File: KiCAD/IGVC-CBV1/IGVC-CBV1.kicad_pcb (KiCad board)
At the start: 2 copper layers, 9.8 x 4.5 mm, 42 parts, among them IC1 STM32F407ZGT6, IC2 SPX3819M5-L-3-3_TR, IC3 AT45DB081E-SSHN-B, J1 STLINKV2 PINS (2.54mm Pitch), J2 Motor Driver Pins (2.54mm Pit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, J3 12401948E412A, J4 Conn_01x02, SW1 SW_SPDT, Y1 EB2532YA12-25.000M_TR

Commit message: placed some things where they need to go
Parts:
- IC2, J4: moved to B.Cu
- moved J1 88.7 mm to (223.2, 80.2), turned to 90 degrees
- moved J2 87.9 mm to (223.1, 92.9), turned to 90 degrees
- moved IC3 72.1 mm to (222.9, 68.1), turned to 90 degrees
- moved R6 68.2 mm to (220.8, 62.9), turned to 90 degrees
- moved SW1 68.1 mm to (200.9, 60.1), turned to 90 degrees
- moved R7 64.8 mm to (222.3, 73.3), turned to 90 degrees
- moved R5 61.7 mm to (220.9, 73.3), turned to 90 degrees
- moved IC1 59.1 mm to (196.8, 89.6)
- moved C18 45.3 mm to (187.0, 72.6), turned to -90 degrees
- moved C22 41.2 mm to (119.4, 81.6), turned to -90 degrees
- moved C17 39.9 mm to (181.7, 72.6), turned to -90 degrees
- moved IC2 36.5 mm to (177.6, 102.3)
- moved C24 32.3 mm to (181.3, 104.5), turned to -90 degrees
- moved C23 32.3 mm to (181.3, 100.4), turned to -90 degrees
- moved FB1 28.1 mm to (184.4, 72.3)
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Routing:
- added copper zone on B.Cu, net (none)
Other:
- board size 9.8 x 4.5 mm -> 4.5 x 9.8 mm

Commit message: finished layout
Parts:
- R8: moved to B.Cu
- moved C22 107.0 mm to (224.1, 59.7), turned to 180 degrees
- moved R8 92.7 mm to (227.7, 68.0), turned to 90 degrees
- moved C21 83.8 mm to (224.1, 61.8), turned to 180 degrees
- moved R1 58.8 mm to (191.4, 72.5), turned to -90 degrees
- moved C1 46.6 mm to (133.3, 71.4), turned to -90 degrees
- moved R3 41.3 mm to (168.7, 88.3), turned to 180 degrees
- moved C16 31.3 mm to (179.2, 72.5), turned to -90 degrees
- moved J4 30.0 mm to (150.9, 98.8), turned to 0 degrees
- moved R10 21.8 mm to (144.5, 87.5)
- moved C15 21.4 mm to (182.5, 93.9)
- moved R9 21.2 mm to (144.4, 83.9)
- moved C19 14.8 mm to (182.3, 90.2), turned to -90 degrees
- moved SW1 13.5 mm to (187.4, 60.5)
- moved C20 6.80 mm to (172.8, 88.4), turned to -90 degrees
- moved Y1 4.80 mm to (177.5, 89.3)
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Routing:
- added copper zone on B.Cu, net GND
- removed copper zone on B.Cu, net (none)

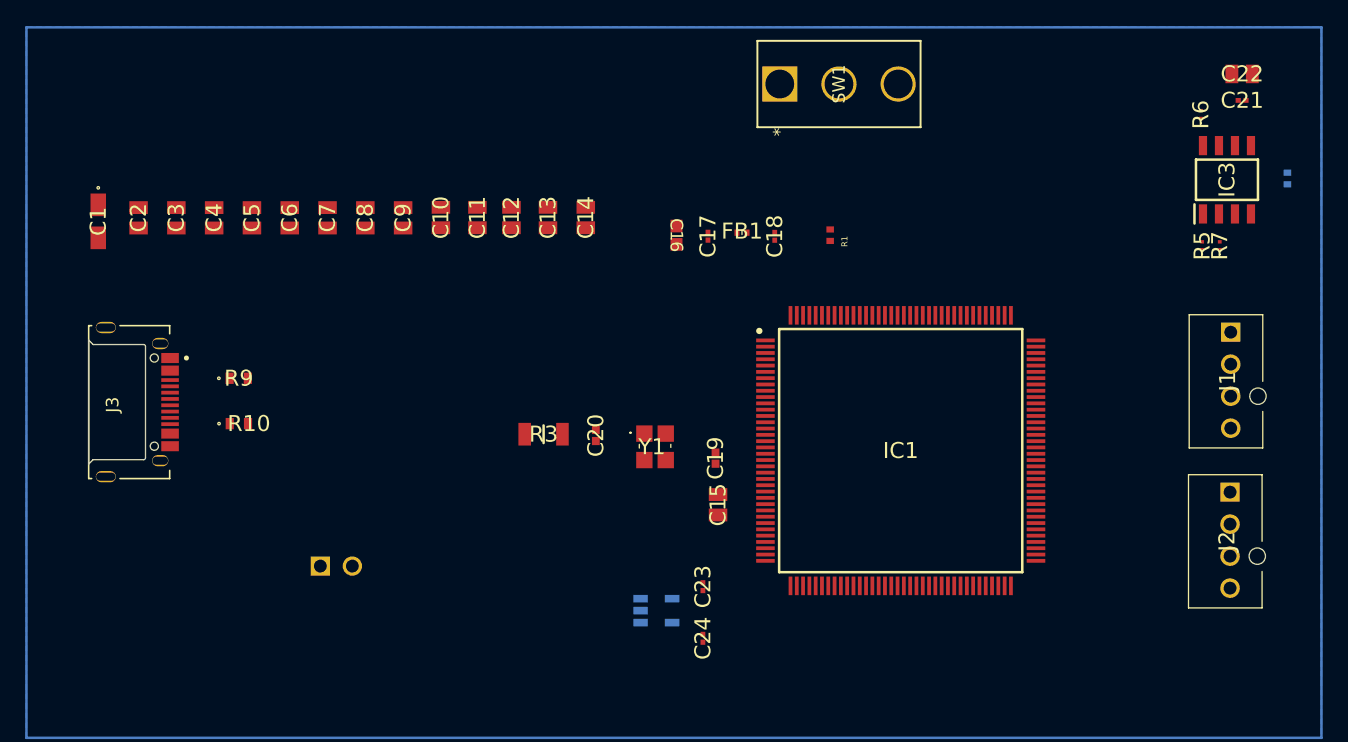
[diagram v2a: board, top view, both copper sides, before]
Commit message: Finished PCB Traces
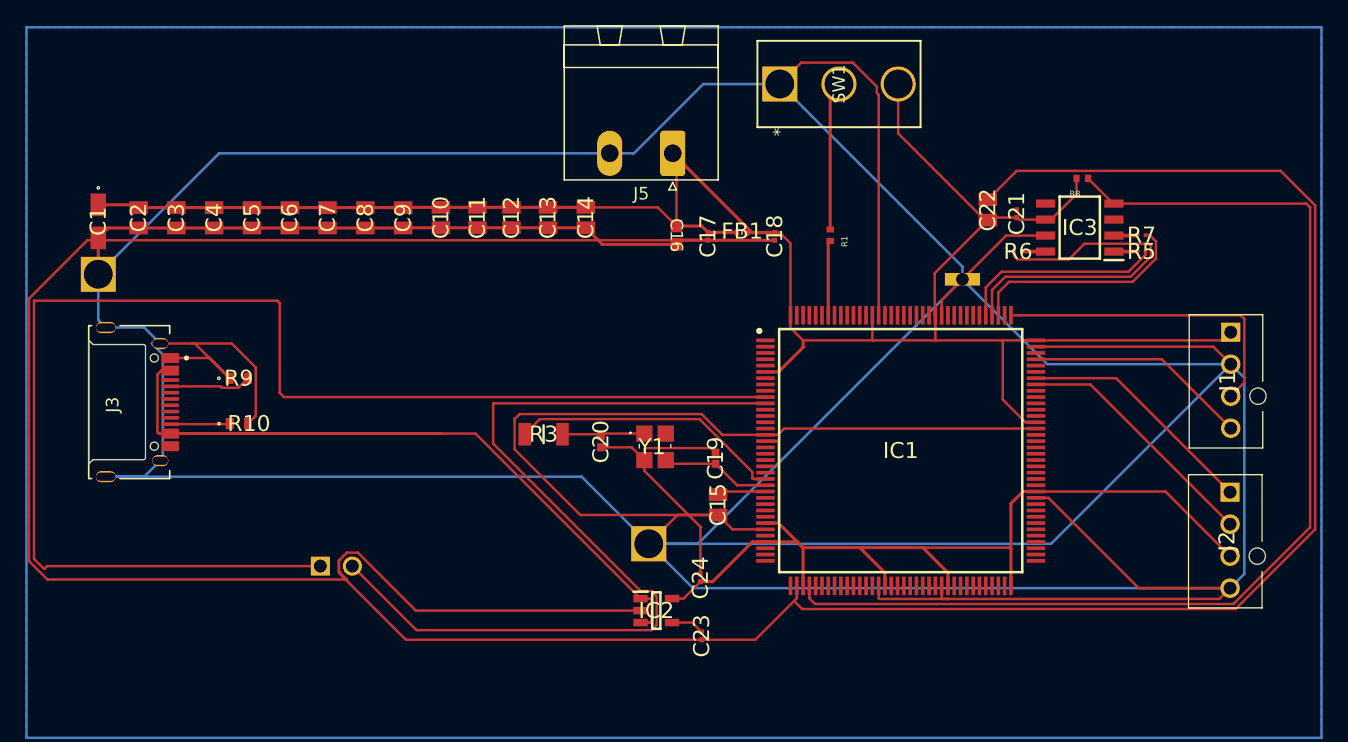
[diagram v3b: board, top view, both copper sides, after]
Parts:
- added ?: , , F.Cu at (133.3, 75.6)
- added ?: , , F.Cu at (201.9, 76.0)
- added ?: , , F.Cu at (177.0, 97.0)
- added J5: Screw_Terminal_01x02, Connector_Phoenix_MSTB:PhoenixContact_MSTBA_2,5_2-G_1x02_P5.00mm_Horizontal, F.Cu at (178.9, 66.0)
- IC2, R8: moved to F.Cu
- moved C22 22.9 mm to (203.9, 70.5), turned to 90 degrees
- moved C21 20.0 mm to (206.2, 70.8), turned to 90 degrees
- moved R6 18.1 mm to (206.3, 73.8), turned to 0 degrees
- moved R8 16.3 mm to (211.4, 68.0), turned to 180 degrees
- moved IC3 12.3 mm to (211.2, 71.9), turned to 180 degrees
- moved R7 6.27 mm to (216.1, 72.5), turned to 0 degrees
- moved R5 4.84 mm to (216.1, 73.8), turned to 0 degrees
- moved C24 4.80 mm to (181.1, 99.7), turned to 90 degrees
- moved C23 3.91 mm to (181.2, 104.3), turned to 90 degrees
- moved C20 0.64 mm to (173.2, 88.9), turned to 90 degrees
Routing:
- net GND: track 0.00 -> 883.5 mm
- net +3.3V: track 0.00 -> 243.0 mm
- net I2C2_SDA: track 0.00 -> 109.1 mm
- net SPI3_NSS: track 0.00 -> 87.4 mm
- net VBUS: track 0.00 -> 74.6 mm
- net I2C2_SCL: track 0.00 -> 71.5 mm
- net SPI3_MISO: track 0.00 -> 28.5 mm
- net SWCLK: track 0.00 -> 25.2 mm
- net RCC_OSC_IN: track 0.00 -> 21.9 mm
- net USART1_TX: track 0.00 -> 20.0 mm
- net USART1_RX: track 0.00 -> 19.2 mm
- net SPI3_SCK: track 0.00 -> 17.8 mm
- net SWDIO: track 0.00 -> 17.7 mm
- net SPI3_MOSI: track 0.00 -> 16.2 mm
- net /SW_BOOT0: track 0.00 -> 11.8 mm
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
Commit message: PCB Update
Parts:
- removed ? (x3): , 
- removed C21: 1uF, LIB_GRMMDXR60J105ME05D:CAPC0502X28N
- removed C22: .1uF, LIB_08051C104K4Z2A:CAPC2012X140N
- removed IC3: AT45DB081E-SSHN-B, LIB_AT45DB081E-SSHN-B:SOIC127P600X175-8N
- removed R5, R6, R7: 0 Ohm, LIB_ERJ-1GJ0R00C:ERJ1G_1023
- removed R8: 10k, RC0402FR-0710KL:RESC1005X40N
- J4: moved to F.Cu
- moved J5 67.3 mm to (115.6, 88.6), turned to -90 degrees
- moved C18 64.7 mm to (140.7, 117.8), turned to 180 degrees
- moved FB1 61.3 mm to (140.7, 115.3), turned to 90 degrees
- moved J1 59.7 mm to (163.6, 83.5), turned to 180 degrees
- moved C17 56.5 mm to (140.7, 111.4), turned to 180 degrees
- moved C16 56.0 mm to (140.2, 112.7), turned to 180 degrees
- moved Y1 48.3 mm to (133.3, 108.9), turned to -90 degrees
- moved C14 47.3 mm to (129.0, 90.9)
- moved C19 46.5 mm to (139.8, 108.9), turned to 180 degrees
- moved J2 43.7 mm to (179.8, 98.7)
- moved R1 42.2 mm to (152.4, 88.6)
- moved C13 42.1 mm to (131.8, 90.9)
- moved IC1 41.0 mm to (158.5, 103.8)
- moved C15 41.0 mm to (144.5, 109.4)
- moved C20 38.6 mm to (138.2, 105.1), turned to -90 degrees
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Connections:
- IC1 pad 111: SPI3_SCK -> unconnected-(IC1-PC10-Pad111)
- IC1 pad 112: SPI3_MISO -> unconnected-(IC1-PC11-Pad112)
- IC1 pad 113: SPI3_MOSI -> unconnected-(IC1-PC12-Pad113)
- IC1 pad 40: SPI3_NSS -> unconnected-(IC1-PA4-Pad40)
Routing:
- net GND: track 883.5 -> 316.4 mm, vias 0 -> 5
- net I2C2_SDA: track 109.1 -> 16.3 mm
- net SPI3_NSS: track 87.4 -> 0.00 mm
- net +3.3V: track 243.0 -> 309.5 mm, vias 0 -> 3
- net VBUS: track 74.6 -> 15.8 mm
- net I2C2_SCL: track 71.5 -> 15.4 mm
- net SPI3_MISO: track 28.5 -> 0.00 mm
- net SPI3_SCK: track 17.8 -> 0.00 mm
- net RCC_OSC_IN: track 21.9 -> 5.48 mm
- net SPI3_MOSI: track 16.2 -> 0.00 mm
- net SWCLK: track 25.2 -> 11.0 mm
- net RCC_OSC_OUT: track 8.74 -> 20.5 mm
- net USART1_RX: track 19.2 -> 10.9 mm
- net /SW_BOOT0: track 11.8 -> 4.68 mm
- net USART1_TX: track 20.0 -> 13.2 mm
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- removed copper zone on B.Cu, net GND
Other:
- board size 4.5 x 9.8 mm -> 85.9 x 67.1 mm
- board text added: "IGVC Project Genesis V1 2023 (Evan E, Colby M., Kerwin Z., Tarun ?)"

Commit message: Finishing Touches on PCB
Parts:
- moved C24 0.46 mm to (161.0, 74.2)
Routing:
- net GND: track 316.4 -> 314.3 mm
- added copper zone on B.Cu, net GND
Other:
- board text added: "IGVC Project Genesis V1 2023 (Evan E, Colby M., Kerwin Z., Tarun Daggolu)"
- board text removed: "IGVC Project Genesis V1 2023 (Evan E, Colby M., Kerwin Z., Tarun ?)"

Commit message: fixed names
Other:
- board text added: "IGVC Project Genesis V1 2023 (Evan E, Colby M, Kerwin Z, Tarun D)"
- board text removed: "IGVC Project Genesis V1 2023 (Evan E, Colby M., Kerwin Z., Tarun Daggolu)"
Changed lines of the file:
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@@
   (gr_rect (start 101.6 54.356) (end 187.452 121.412)
     (stroke (width 0.1) (type default)) (fill none) (layer "Edge.Cuts"))
-  (gr_text "IGVC Project Genesis V1\n2023\n(Evan E, Colby M., Kerwin Z., Tarun Daggolu)" (at 122.2 68) (layer "F.SilkS")
+  (gr_text "IGVC Project Genesis V1\n2023\n(Evan E, Colby M, Kerwin Z, Tarun D)" (at 122.2 68) (layer "F.SilkS")
     (effects (font (size 1.5 1) (thickness 0.25) bold) (justify bottom))
   )
